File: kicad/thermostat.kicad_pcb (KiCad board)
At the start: 2 copper layers, 100.5 x 79.5 mm, 80 parts, among them IC1 LM2596S-5, J1 Conn_01x05, J2 Conn_02x02_Top_Bottom, J3 Conn_01x04, J4 Conn_01x04, J6 Screw_Terminal_01x05, SW1 Button, SW2 Button, SW3 Button, SW4 Button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

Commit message: updates
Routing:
- net /PWR_5V_RAW: track 167.3 -> 110.4 mm, vias 0 -> 1
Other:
- board text added: "Button Board"
- board text added: "LCD w/ Optional Power"
- board text added: "Main Board"
- board text added: "Power Jumper"

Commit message: design v2.2 sent to fab
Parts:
- D40, D41, D44, D45, D46, D47: value LED -> LED Green
- D42: value LED -> LED REd
- D43: value LED -> LED Blue
- D51, D52: value LTRB-RASF -> LED RGB
- RELAY1: value RELAY_FAN -> RELAY
- RELAY2: value RELAY_HEAT -> RELAY
- RELAY3: value RELAY_COOL -> RELAY

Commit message: change of silkscreen to reflect v3.0
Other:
- board text added: "RPT v3.0 March 2020 mike@madllama.net"
- board text removed: "RPT v2.1 February 2020 mike@madllama.net"

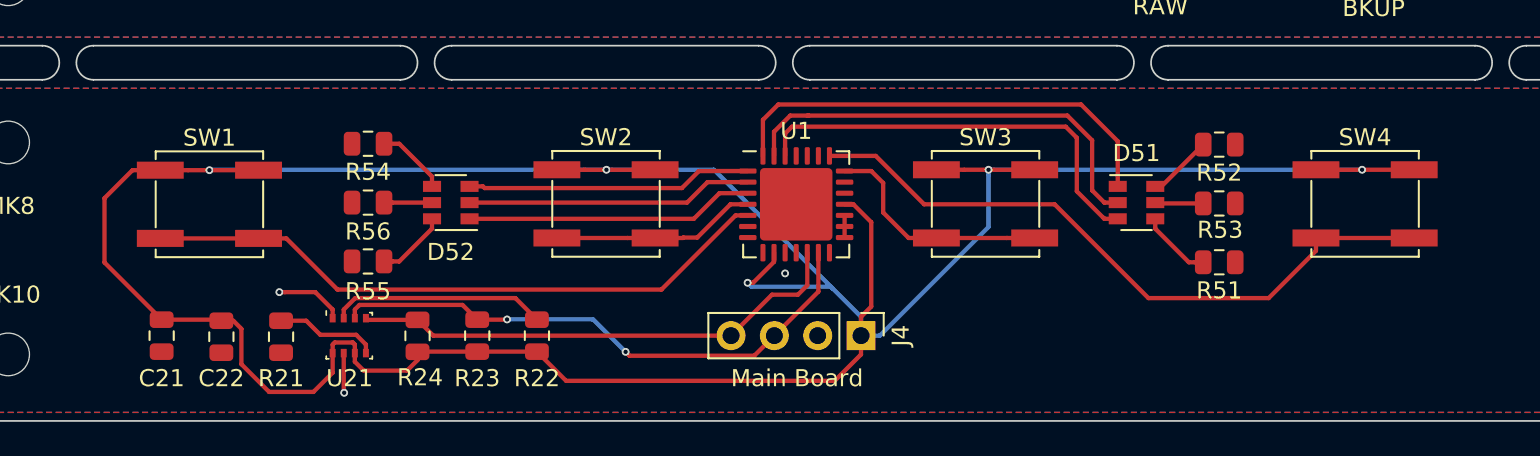
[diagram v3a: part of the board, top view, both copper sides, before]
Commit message: updates, cad broken
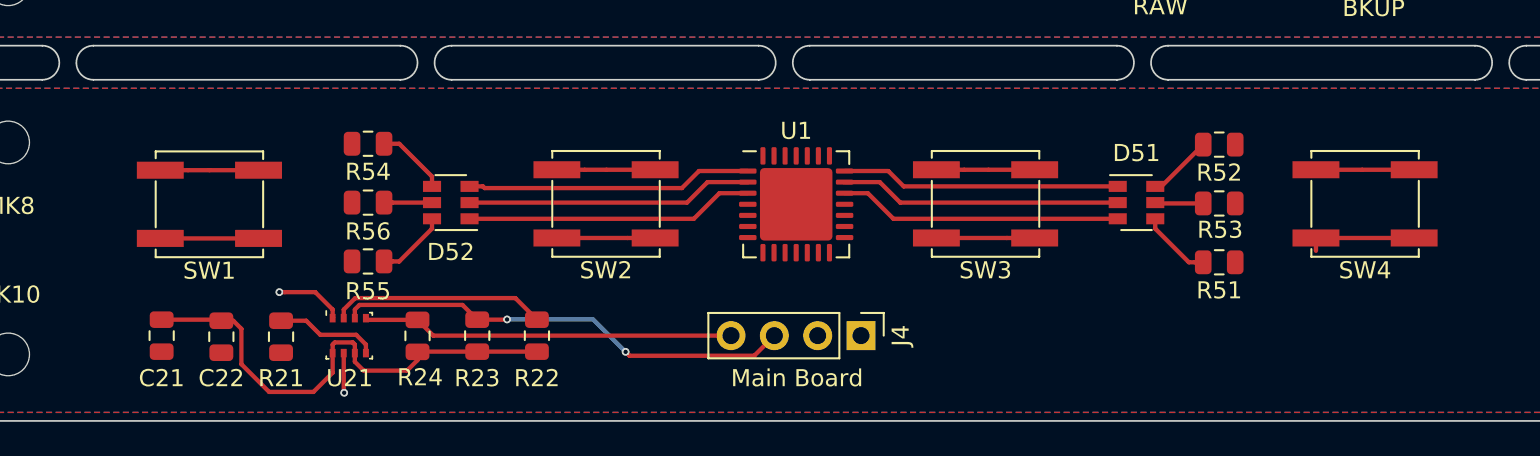
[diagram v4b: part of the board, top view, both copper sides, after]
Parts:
- D40, D41, D44, D45, D46, D47: value LED Green -> Green
- D42: value LED REd -> Red
- D43: value LED Blue -> Blue
- D51, D52: value LED RGB -> RGB
- turned SW1 to 180 degrees
- turned SW2 to 180 degrees
- turned SW3 to 180 degrees
- turned SW4 to 180 degrees
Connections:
- U1 pad 10: /BTNS_GND -> (no net)
- U1 pad 11: (no net) -> /BTNS_SDA
- U1 pad 13: /BTNS_SDA -> (no net)
- U1 pad 15: /BTNS_GND -> (no net)
- U1 pad 16: /BTNS_GND -> (no net)
- U1 pad 17: /BTNS_GND -> (no net)
- U1 pad 18: /BTNS_PWR_3V3 -> (no net)
- U1 pad 19: (no net) -> Net-(D51-Pad3)
- U1 pad 20: (no net) -> Net-(D51-Pad2)
- U1 pad 21: Net-(SW3-Pad2) -> Net-(D51-Pad1)
- U1 pad 22: Net-(SW4-Pad2) -> (no net)
- U1 pad 26: Net-(D51-Pad3) -> (no net)
- U1 pad 27: Net-(D51-Pad2) -> (no net)
- U1 pad 28: Net-(D51-Pad1) -> (no net)
- U1 pad 29: (no net) -> /BTNS_PWR_3V3
- U1 pad 4: Net-(SW2-Pad2) -> (no net)
- U1 pad 5: Net-(SW1-Pad2) -> /BTNS_GND
- U1 pad 6: (no net) -> /BTNS_PWR_3V3
- U1 pad 8: (no net) -> /BTNS_GND
- U1 pad 9: /BTNS_PWR_3V3 -> /BTNS_GND
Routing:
- net /BTNS_PWR_3V3: track 181.0 -> 53.0 mm, vias 5 -> 0
- net Net-(SW4-Pad2): track 39.6 -> 5.76 mm
- net Net-(SW1-Pad2): track 37.5 -> 5.76 mm
- net Net-(D51-Pad1): track 26.8 -> 16.4 mm
- net Net-(D51-Pad2): track 25.9 -> 16.5 mm
- net Net-(D51-Pad3): track 25.1 -> 16.6 mm
- net Net-(SW3-Pad2): track 13.8 -> 5.76 mm
- net /BTNS_SCL: track 29.4 -> 21.8 mm
- net Net-(SW2-Pad2): track 12.0 -> 5.76 mm
- net /BTNS_SDA: track 32.9 -> 26.9 mm
- net /BTNS_GND: track 7.72 -> 6.42 mm, vias 3 -> 2

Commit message: Re-route 23017
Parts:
- turned SW1 to 0 degrees
- turned SW2 to 0 degrees
- turned SW3 to 0 degrees
- turned SW4 to 0 degrees
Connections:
- SW1 pad 1: /BTNS_PWR_3V3 -> Net-(SW1-Pad1)
- SW1 pad 2: Net-(SW1-Pad2) -> /BTNS_GND
- SW2 pad 1: /BTNS_PWR_3V3 -> Net-(SW2-Pad1)
- SW2 pad 2: Net-(SW2-Pad2) -> /BTNS_GND
- SW3 pad 1: /BTNS_PWR_3V3 -> Net-(SW3-Pad1)
- SW3 pad 2: Net-(SW3-Pad2) -> /BTNS_GND
- SW4 pad 1: /BTNS_PWR_3V3 -> Net-(SW4-Pad1)
- SW4 pad 2: Net-(SW4-Pad2) -> /BTNS_GND
- U1 pad 11: /BTNS_SDA -> /BTNS_GND
- U1 pad 12: /BTNS_SCL -> /BTNS_GND
- U1 pad 13: (no net) -> /BTNS_GND
- U1 pad 14: (no net) -> /BTNS_PWR_3V3
- U1 pad 22: (no net) -> Net-(SW3-Pad1)
- U1 pad 23: (no net) -> Net-(SW4-Pad1)
- U1 pad 27: (no net) -> Net-(SW1-Pad1)
- U1 pad 28: (no net) -> Net-(SW2-Pad1)
- U1 pad 29: /BTNS_PWR_3V3 -> /BTNS_GND
- U1 pad 5: /BTNS_GND -> /BTNS_PWR_3V3
- U1 pad 6: /BTNS_PWR_3V3 -> /BTNS_GND
- U1 pad 8: /BTNS_GND -> /BTNS_SCL
- U1 pad 9: /BTNS_GND -> /BTNS_SDA
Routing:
- net Net-(SW1-Pad1): track 0.00 -> 39.6 mm
- net Net-(SW4-Pad1): track 0.00 -> 38.6 mm
- net /BTNS_GND: track 6.42 -> 37.4 mm, vias 2 -> 5
- net /BTNS_PWR_3V3: track 53.0 -> 71.2 mm, vias 0 -> 2
- net Net-(SW2-Pad1): track 0.00 -> 13.8 mm
- net Net-(SW3-Pad1): track 0.00 -> 13.7 mm
- net Net-(SW4-Pad2): track 5.76 -> 0.00 mm
- net Net-(SW3-Pad2): track 5.76 -> 0.00 mm
- net Net-(SW2-Pad2): track 5.76 -> 0.00 mm
- net Net-(SW1-Pad2): track 5.76 -> 0.00 mm
- net /BTNS_SCL: track 21.8 -> 27.5 mm
- net /BTNS_SDA: track 26.9 -> 32.2 mm, vias 2 -> 1

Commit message: routed board
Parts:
- removed C11: 25F, Capacitor_THT:CP_Radial_D18.0mm_P7.50mm
- removed C12: 2.2uF, Capacitor_SMD:C_0805_2012Metric
- removed C13, C14: 100uF, Capacitor_SMD:C_0805_2012Metric
- removed C15, C16: 100nF, Capacitor_SMD:C_0805_2012Metric
- removed D44, D45, D46: Green, LED_SMD:LED_0805_2012Metric
- removed L2: 2.2uH, Inductor_SMD:L_Coilcraft_XAL5030
- removed R10: 120k, Resistor_SMD:R_0805_2012Metric
- removed R11: 39k, Resistor_SMD:R_0805_2012Metric
- removed R12, R44, R45, R46: 1k, Resistor_SMD:R_0805_2012Metric
- removed R13: 294k, Resistor_SMD:R_0805_2012Metric
- removed R14: 698k, Resistor_SMD:R_0805_2012Metric
- removed R15: 1050k, Resistor_SMD:R_0805_2012Metric
- removed R16: 200k, Resistor_SMD:R_0805_2012Metric
- removed R18: 10m, Resistor_SMD:R_0805_2012Metric
- removed T1, T2: SIR434DN, Package_SO:Vishay_PowerPAK_1212-8_Single
- removed U11: LTC4041, project_footprints:ltc4041
- added R57: 10k, Resistor_SMD:R_0805_2012Metric, F.Cu at (210.0, 189.9)
- J1: value Conn_01x05 -> Conn_01x04; footprint Connector_PinHeader_2.54mm:PinHeader_1x05_P2.54mm_Vertical -> Connector_PinHeader_2.54mm:PinHeader_1x04_P2.54mm_Vertical
- J2: value Conn_02x02_Top_Bottom -> Conn_01x03; footprint Connector_PinHeader_2.54mm:PinHeader_2x02_P2.54mm_Vertical -> Connector_PinHeader_2.54mm:PinHeader_1x03_P2.54mm_Vertical
- J3, J4: value Conn_01x04 -> Conn_01x05; footprint Connector_PinHeader_2.54mm:PinHeader_1x04_P2.54mm_Vertical -> Connector_PinHeader_2.54mm:PinHeader_1x05_P2.54mm_Vertical
- MK5: footprint MountingHole:MountingHole_5mm_Pad -> MountingHole:MountingHole_5mm
- moved J1 85.6 mm to (160.5, 157.5)
- moved J3 85.2 mm to (154.0, 155.0)
- moved D1 64.4 mm to (171.5, 170.5), turned to 270 degrees
- moved D2 50.7 mm to (179.0, 170.0), turned to 270 degrees
- moved C1 49.3 mm to (190.4, 167.8)
- moved J2 46.6 mm to (160.5, 172.0)
- moved Pi1 26.2 mm to (217.5, 131.5)
- moved CONN1 25.9 mm to (193.0, 141.9)
- moved R47 25.4 mm to (241.5, 166.0)
- moved D47 25.0 mm to (246.3, 166.0)
- moved J6 23.7 mm to (176.5, 163.0), turned to 90 degrees
- moved MK1 22.0 mm to (154.0, 143.0)
- moved MK2 22.0 mm to (246.5, 143.0)
- moved L1 21.0 mm to (214.0, 168.0), turned to 270 degrees
- moved D41 19.1 mm to (197.0, 151.1)
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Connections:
- CONN1 pad 11: (no net) -> /GPIO17(GEN0)
- CONN1 pad 37: /GPIO26 -> (no net)
- J1 pad 2: Net-(J1-Pad2) -> /PWR_5V
- J1 pad 3: /PWR_5V -> /GPIO2(SDA1)
- J1 pad 4: /GPIO2(SDA1) -> /GPIO3(SCL1)
- J2 pad 3: /PWR_CAP_IN -> GND
- J3 pad 1: /PWR_3.3V -> /GPIO17(GEN0)
- J3 pad 2: GND -> /PWR_3.3V
- J3 pad 3: /GPIO2(SDA1) -> GND
- J3 pad 4: /GPIO3(SCL1) -> /GPIO2(SDA1)
- J4 pad 1: /BTNS_PWR_3V3 -> /BTNS_INT
- J4 pad 2: /BTNS_GND -> /BTNS_PWR_3V3
- J4 pad 3: /BTNS_SDA -> /BTNS_GND
- J4 pad 4: /BTNS_SCL -> /BTNS_SDA
- U1 pad 16: (no net) -> Net-(R57-Pad2)
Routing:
- net /PWR_CAP_OUT: track 100.2 -> 0.00 mm
- net Net-(C11-Pad1): track 95.8 -> 0.00 mm, vias 2 -> 0
- net /PWR_5V: track 204.7 -> 126.8 mm, vias 4 -> 3
- net /PWR_CAP_IN: track 65.2 -> 0.00 mm, vias 2 -> 0
- net /GPIO2(SDA1): track 116.2 -> 51.1 mm
- net /GPIO17(GEN0): track 0.00 -> 63.1 mm
- net Net-(R18-Pad1): track 62.8 -> 0.00 mm, vias 2 -> 0
- net /GPIO3(SCL1): track 101.0 -> 54.7 mm
- net Net-(C1-Pad1): track 20.8 -> 58.0 mm
- net Net-(R15-Pad1): track 32.1 -> 0.00 mm, vias 4 -> 0
- net Net-(R13-Pad1): track 30.4 -> 0.00 mm, vias 2 -> 0
- net Net-(J1-Pad2): track 29.2 -> 0.00 mm
- net /SYSGD: track 26.2 -> 0.00 mm, vias 2 -> 0
- net Net-(D2-Pad1): track 23.9 -> 49.6 mm
- net /BTNS_PWR_3V3: track 71.2 -> 94.0 mm, vias 2 -> 7
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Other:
- board size 100.5 x 79.5 mm -> 99.5 x 54 mm
- board text added: "LCD Display"
- board text removed: "CAP"
- board text removed: "LCD w/ Optional Power"
- board text removed: "PFO"
- board text removed: "SYS"

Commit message: final submission to OSH Park
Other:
- board text added: "RPT v4.0 April 2020 mike@madllama.net"
- board text removed: "RPT v3.0 March 2020 mike@madllama.net"
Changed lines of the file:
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@@
   )
   (layers
-    (0 F.Cu signal)
-    (31 B.Cu signal hide)
+    (0 F.Cu signal hide)
+    (31 B.Cu signal)
     (32 B.Adhes user hide)
     (33 F.Adhes user hide)
-    (34 B.Paste user hide)
-    (35 F.Paste user)
-    (36 B.SilkS user hide)
-    (37 F.SilkS user)
-    (38 B.Mask user hide)
-    (39 F.Mask user)
+    (34 B.Paste user)
+    (35 F.Paste user hide)
+    (36 B.SilkS user)
+    (37 F.SilkS user hide)
+    (38 B.Mask user)
+    (39 F.Mask user hide)
     (40 Dwgs.User user hide)
     (41 Cmts.User user hide)
@@
     (44 Edge.Cuts user)
     (45 Margin user hide)
-    (46 B.CrtYd user hide)
-    (47 F.CrtYd user)
-    (48 B.Fab user hide)
+    (46 B.CrtYd user)
+    (47 F.CrtYd user hide)
+    (48 B.Fab user)
     (49 F.Fab user hide)
   )
@@
     (effects (font (size 1 1) (thickness 0.15)))
   )
-  (gr_text "RPT v3.0 March 2020\nmike@madllama.net" (at 232.85 170.7) (layer B.SilkS)
+  (gr_text "RPT v4.0 April 2020\nmike@madllama.net" (at 232.85 170.7) (layer B.SilkS)
     (effects (font (size 1 1) (thickness 0.15)) (justify mirror))
   )

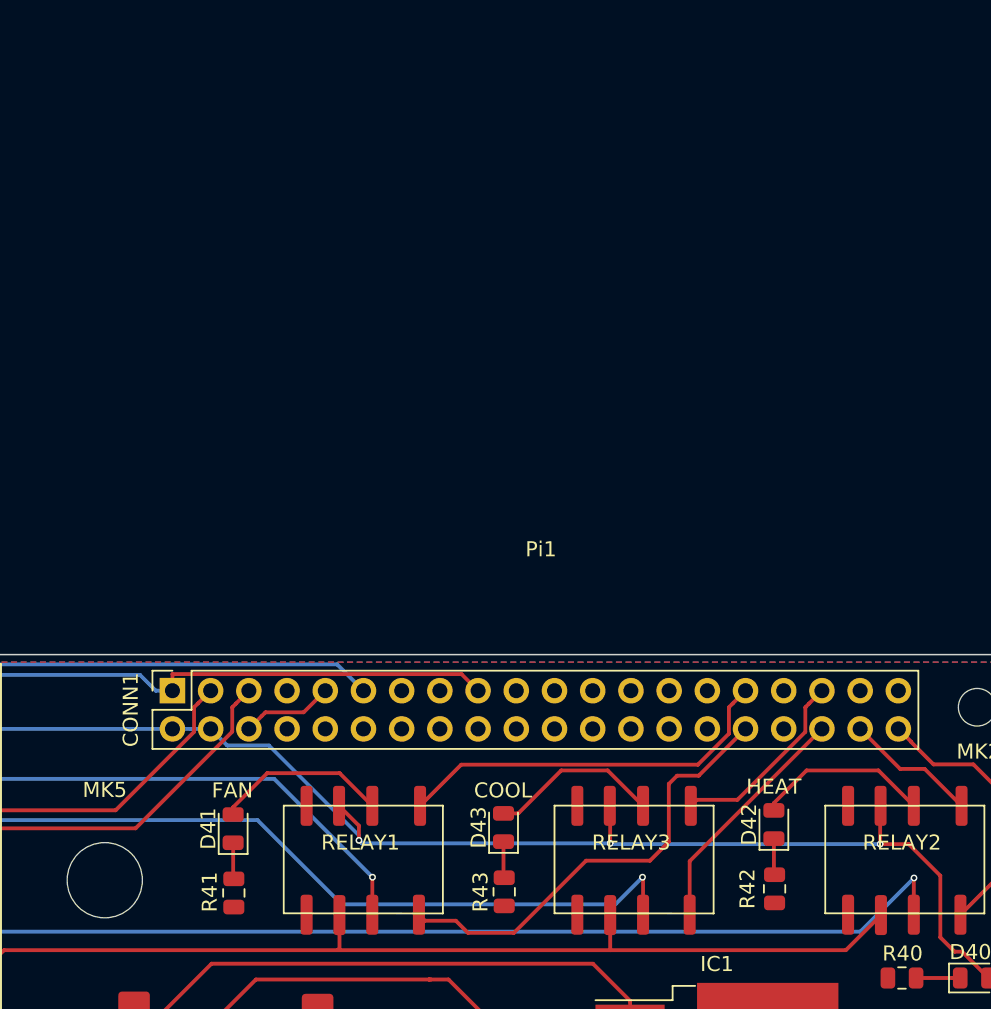
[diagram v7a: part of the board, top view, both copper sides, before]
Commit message: new relay driver circuitry, layout needed
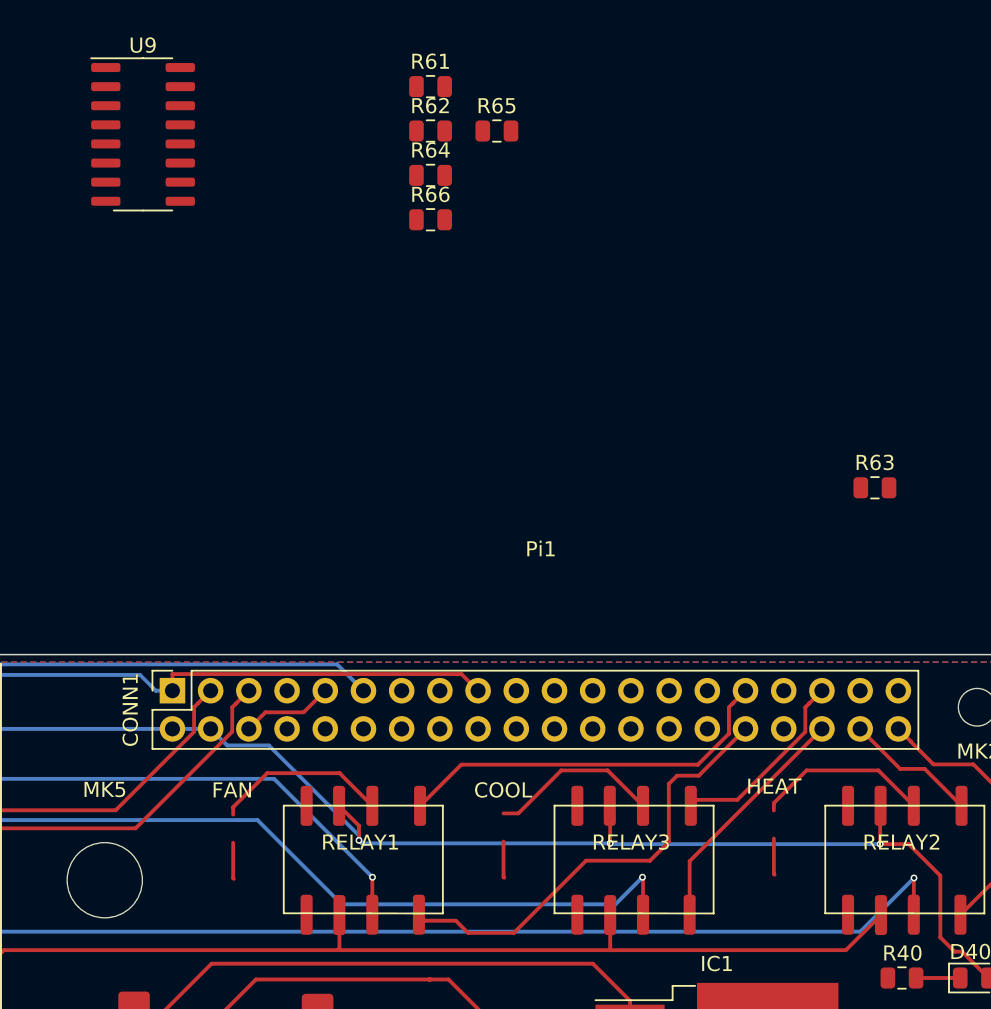
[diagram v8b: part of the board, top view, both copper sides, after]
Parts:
- removed D41: Green, LED_SMD:LED_0805_2012Metric
- removed D42: Red, LED_SMD:LED_0805_2012Metric
- removed D43: Blue, LED_SMD:LED_0805_2012Metric
- removed R41, R42, R43: 1k, Resistor_SMD:R_0805_2012Metric
- added R61: 64, Resistor_SMD:R_0805_2012Metric, F.Cu at (210.2, 101.7)
- added R62: 64, Resistor_SMD:R_0805_2012Metric, F.Cu at (210.2, 104.7)
- added R63: 64, Resistor_SMD:R_0805_2012Metric, F.Cu at (239.7, 128.4)
- added R64: 64, Resistor_SMD:R_0805_2012Metric, F.Cu at (210.2, 107.6)
- added R65: 64, Resistor_SMD:R_0805_2012Metric, F.Cu at (214.6, 104.7)
- added R66: 64, Resistor_SMD:R_0805_2012Metric, F.Cu at (210.2, 110.6)
- added U9: ULN2003AD, Package_SO:SOIC-16_3.9x9.9mm_P1.27mm, F.Cu at (191.0, 104.9)
- RELAY1: value RELAY -> FAN
- RELAY2: value RELAY -> HEAT
- RELAY3: value RELAY -> COOL
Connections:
- RELAY1 pad 1: /GPIO6 -> Net-(R64-Pad1)
- RELAY1 pad 2: /IND_FAN -> (no net)
- RELAY1 pad 3: /PWR_5V -> GND
- RELAY1 pad 8: /GPIO12(PWM0) -> Net-(R61-Pad2)
- RELAY2 pad 1: /GPIO20(SPI1_MOSI) -> Net-(R65-Pad1)
- RELAY2 pad 2: /IND_HEAT -> (no net)
- RELAY2 pad 3: /PWR_5V -> GND
- RELAY2 pad 8: /GPIO21(SPI1_SCK) -> Net-(R62-Pad2)
- RELAY3 pad 1: /GPIO19(SPI1_MISO) -> Net-(R66-Pad1)
- RELAY3 pad 2: /IND_COOL -> (no net)
- RELAY3 pad 3: /PWR_5V -> GND
- RELAY3 pad 8: /GPIO16 -> Net-(R63-Pad2)
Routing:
- net (no net): track 0.00 -> 34.7 mm
- net /IND_HEAT: track 11.7 -> 0.00 mm
- net /IND_FAN: track 11.6 -> 0.00 mm
- net /IND_COOL: track 11.4 -> 0.00 mm
